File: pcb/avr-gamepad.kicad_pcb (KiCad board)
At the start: 2 copper layers, 53.2 x 53 mm, 36 parts, among them J1 Conn_01x08, J2 Conn_01x08, J3 Conn_01x05, P1 USB_C_Plug_USB2.0, SW1 RESET, SW10 Up, SW11 Down, SW12 Left, SW13 Select, SW14 HWB, SW2 R, SW3 X, SW4 A, SW5 B, SW6 Start, SW7 Y, SW8 Right, SW9 L, U1 ATmega32U4-AU, Y1 Crystal_GND24

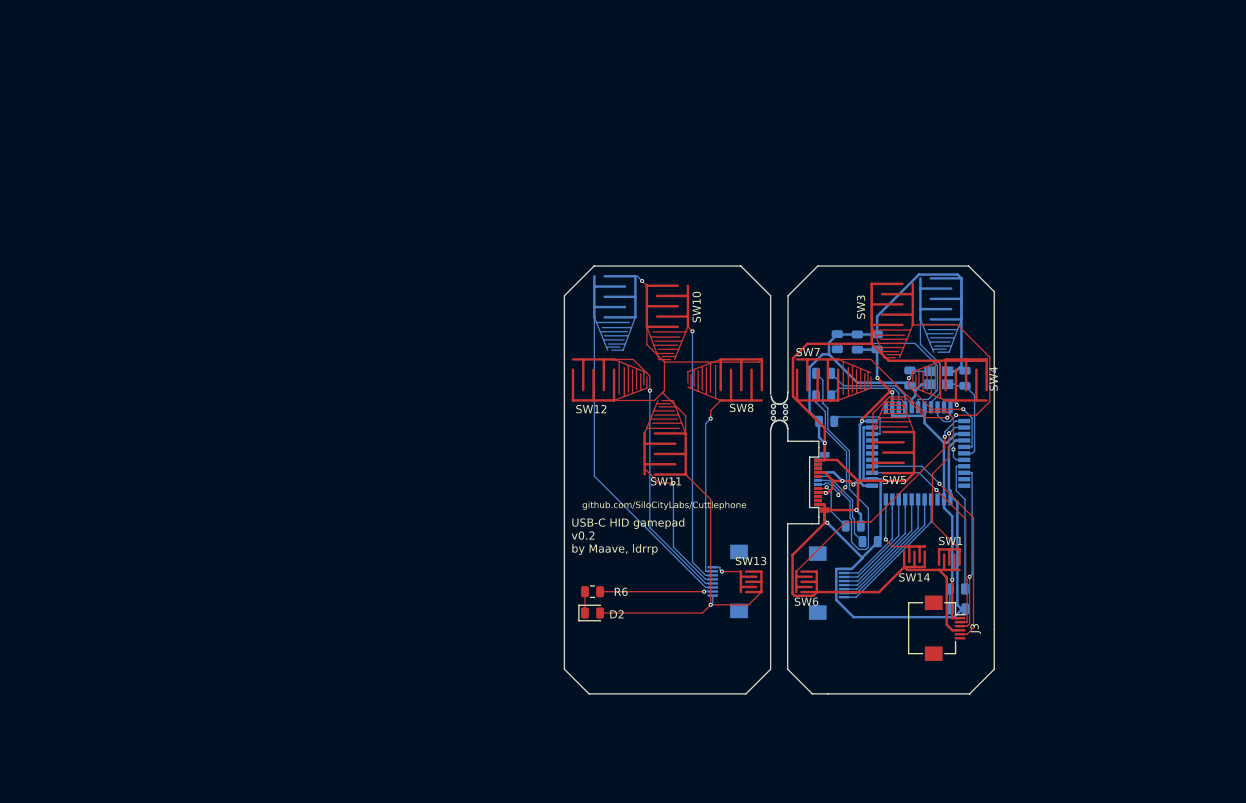
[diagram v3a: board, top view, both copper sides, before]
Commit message: change left/right on schematic, start arranging pcb, add pcf8574 footprint
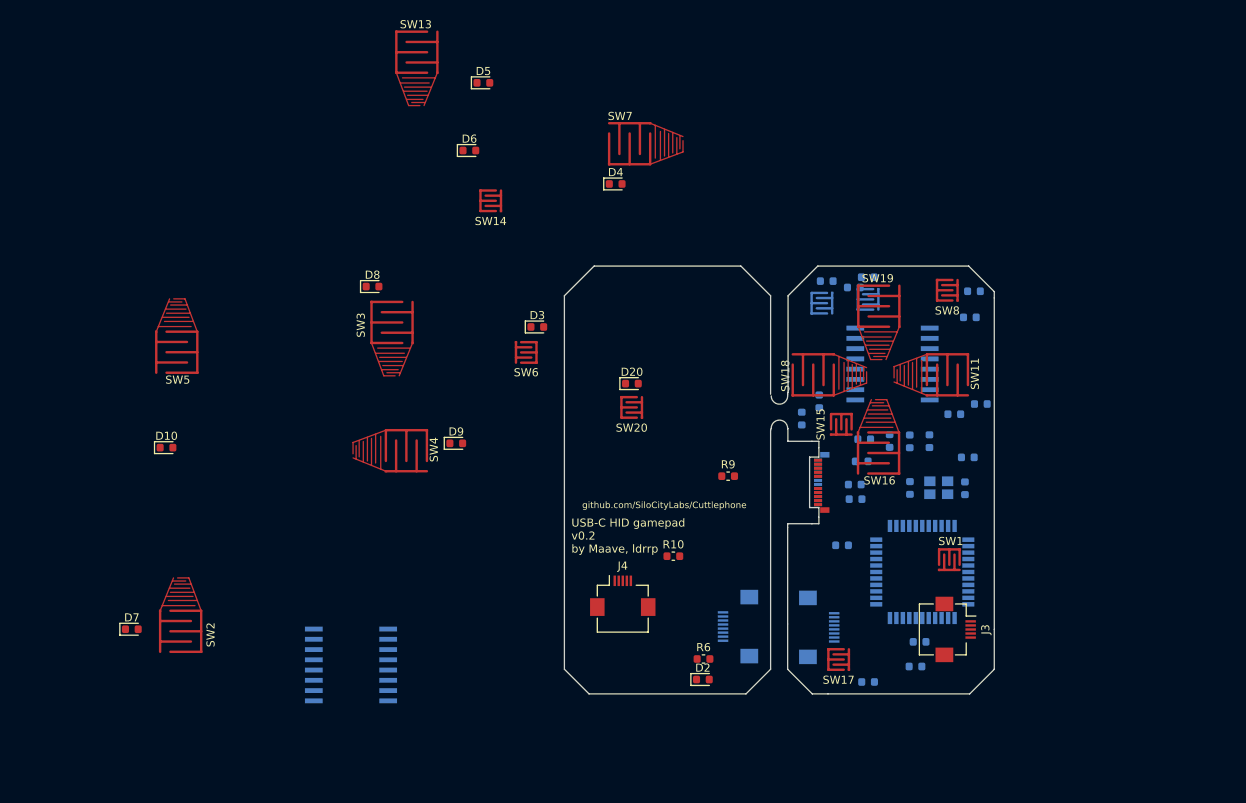
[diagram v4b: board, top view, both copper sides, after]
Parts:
- removed G***: LOGO, squidward:loser_silkscreen
- removed SW12: Left, button-contacts:Large_tapered
- removed mb-2mm-2: mb2, Panelization:mouse-bite-2mm-slot
- added D10: 1N4148, Diode_SMD:D_0603_1608Metric, F.Cu at (50.6, 102.9)
- added D11: 1N4148, Diode_SMD:D_0603_1608Metric, B.Cu at (137.4, 131.9)
- added D12: 1N4148, Diode_SMD:D_0603_1608Metric, B.Cu at (150.5, 83.5)
- added D13: 1N4148, Diode_SMD:D_0603_1608Metric, B.Cu at (132.3, 82.3)
- added D14: 1N4148, Diode_SMD:D_0603_1608Metric, B.Cu at (150.0, 86.7)
- added D15: 1N4148, Diode_SMD:D_0603_1608Metric, B.Cu at (148.1, 98.7)
- added D16: 1N4148, Diode_SMD:D_0603_1608Metric, B.Cu at (137.4, 81.8)
- added D17: 1N4148, Diode_SMD:D_0603_1608Metric, B.Cu at (135.6, 83.0)
- added D18: 1N4148, Diode_SMD:D_0603_1608Metric, B.Cu at (131.4, 97.1)
- added D19: 1N4148, Diode_SMD:D_0603_1608Metric, B.Cu at (129.2, 99.3)
- added D20: 1N4148, Diode_SMD:D_0603_1608Metric, F.Cu at (108.2, 94.9)
- added D3: 1N4148, Diode_SMD:D_0603_1608Metric, F.Cu at (96.5, 87.9)
- added D4: 1N4148, Diode_SMD:D_0603_1608Metric, F.Cu at (106.2, 70.2)
- added D5: 1N4148, Diode_SMD:D_0603_1608Metric, F.Cu at (89.8, 57.7)
- added D6: 1N4148, Diode_SMD:D_0603_1608Metric, F.Cu at (88.1, 66.1)
- added D7: 1N4148, Diode_SMD:D_0603_1608Metric, F.Cu at (46.3, 125.3)
- added D8: 1N4148, Diode_SMD:D_0603_1608Metric, F.Cu at (76.1, 82.9)
- added D9: 1N4148, Diode_SMD:D_0603_1608Metric, F.Cu at (86.4, 102.3)
- added J4: Conn_01x05, uxcell-ffc:uxcell_ffc_0.5pitch_1x05, F.Cu at (107.0, 121.2)
- added R10: 1K, Resistor_SMD:R_0603_1608Metric, F.Cu at (113.3, 116.3)
- added R7: 1K, Resistor_SMD:R_0603_1608Metric, B.Cu at (143.8, 126.9)
- added R8: 1K, Resistor_SMD:R_0603_1608Metric, B.Cu at (143.3, 130.0)
- added R9: 1K, Resistor_SMD:R_0603_1608Metric, F.Cu at (120.1, 106.4)
- added SW15: Custom4, button-contacts:Small, F.Cu at (134.1, 100.0)
- added SW16: B, button-contacts:Large_tapered, F.Cu at (138.7, 103.5)
- added SW17: Start, button-contacts:Small, F.Cu at (133.8, 129.1)
- added SW18: Y, button-contacts:Large_tapered, F.Cu at (130.6, 93.9)
- added SW19: X, button-contacts:Large_tapered, F.Cu at (138.7, 85.4)
- added SW20: Custom2, button-contacts:Small, F.Cu at (108.2, 97.9)
- added U2: PCF8574, pcf8574:SO16W, B.Cu at (73.4, 129.8)
- added U3: PCF8574, pcf8574:SO16W, B.Cu at (140.4, 92.5)
- C1, C2, C3, C4, C5, C6: footprint Capacitor_SMD:C_0805_2012Metric -> Capacitor_SMD:C_0603_1608Metric
- D1, D2: footprint LED_SMD:LED_0805_2012Metric -> LED_SMD:LED_0603_1608Metric
- J1, J2: value Conn_01x08 -> Conn_01x06
- J3: footprint Connector_FFC-FPC:Hirose_FH12-6S-0.5SH_1x06-1MP_P0.50mm_Horizontal -> uxcell-ffc:uxcell_ffc_0.5pitch_1x05
- R1, R2, R3, R4, R5, R6: footprint Resistor_SMD:R_0805_2012Metric -> Resistor_SMD:R_0603_1608Metric
- SW10: value Up -> R2; footprint button-contacts:Large_tapered -> button-contacts:Small; moved to B.Cu
- SW11: value Down -> A
- SW13: value Select -> Left; footprint button-contacts:Small -> button-contacts:Large_tapered
- SW14: value HWB -> L2
- SW2: value R -> Right; moved to F.Cu
- SW3: value X -> Up
- SW4: value A -> Down
- SW5: value B -> Custom1
- SW6: value Start -> Select
- SW7: value Y -> L1
- SW8: value Right -> R1; footprint button-contacts:Large_tapered -> button-contacts:Small
- SW9: value L -> Custom3; footprint button-contacts:Large_tapered -> button-contacts:Small
- moved SW2 102.7 mm to (52.3, 125.6)
- moved SW5 89.6 mm to (51.8, 91.1)
- moved SW13 77.5 mm to (81.6, 53.9), turned to 0 degrees
- moved SW4 69.8 mm to (80.3, 103.3)
- moved SW14 68.5 mm to (90.7, 72.3), turned to 0 degrees
- moved SW3 62.0 mm to (78.5, 87.4)
- moved SW6 44.8 mm to (95.1, 91.1)
- moved SW7 37.4 mm to (107.9, 65.3)
- moved SW11 36.3 mm to (147.2, 93.9), turned to 270 degrees
- moved SW9 31.3 mm to (137.4, 84.5), turned to 0 degrees
- moved SW8 27.8 mm to (147.2, 83.4), turned to 0 degrees
- moved R5 23.1 mm to (151.4, 97.5)
- moved SW10 19.1 mm to (131.7, 85.0)
- moved D1 18.8 mm to (149.8, 104.1)
- moved R6 16.1 mm to (117.0, 129.0)
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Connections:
- net /pd3-21 renamed Net-(U1-Pad21)
- net /pd4-25 renamed Net-(U1-Pad25)
- net /pd5-22 renamed Net-(U1-Pad22)
- net /pe6-1 renamed Net-(U1-Pad1)
- net /pf0-41 renamed Net-(U1-Pad41)
- net /pf1-40 renamed Net-(U1-Pad40)
- net /pf6-37 renamed /JoyRightX
- net /pf7-36 renamed /JoyRightY
- net Net-(R1-Pad1) renamed /D+
- net Net-(R2-Pad1) renamed /D-
- D2 pad 2: Net-(D2-Pad2) -> /GND_L
- J1 pad 1: Net-(J1-Pad1) -> /SDA_L
- J1 pad 2: Net-(J1-Pad2) -> /SCL_L
- J1 pad 3: Net-(J1-Pad3) -> /JoyLeftX_L
- J1 pad 4: Net-(J1-Pad4) -> /JoyLeftY_L
- J1 pad 5: Net-(J1-Pad5) -> /VCC_L
- J1 pad 6: Net-(J1-Pad6) -> /GND_L
- J1 pad 7: Net-(J1-Pad7) -> (no net)
- J1 pad 8: Net-(D2-Pad2) -> (no net)
- J2 pad 1: /pd6-26 -> /SDA
- J2 pad 2: /pd7-27 -> /SCL
- J2 pad 3: /pb4-28 -> /JoyLeftX
- J2 pad 4: /pb5-29 -> /JoyLeftY
- J2 pad 5: /pb6-30 -> +5V
- J2 pad 6: /pc6-31 -> GND
- J2 pad 7: /pc7-32 -> (no net)
- J2 pad 8: GND -> (no net)
- J3 pad 3: /pd2-20 -> /R3
- P1 pad A6: Net-(P1-PadA6) -> Net-(P1-PadA5)
- R1 pad 2: Net-(P1-PadA6) -> Net-(P1-PadA5)
- R5 pad 2: /pd1-19 -> Net-(R5-Pad2)
- R6 pad 2: Net-(J1-Pad7) -> Net-(R6-Pad2)
- SW10 pad 1: Net-(J1-Pad3) -> /Col1
- SW10 pad 2: Net-(D2-Pad2) -> Net-(D13-Pad2)
- SW11 pad 1: Net-(J1-Pad4) -> /Col2
- SW11 pad 2: Net-(D2-Pad2) -> Net-(D14-Pad2)
- SW13 pad 1: Net-(J1-Pad1) -> /ColL1
- SW13 pad 2: Net-(D2-Pad2) -> Net-(D5-Pad2)
- SW14 pad 1: Net-(SW14-Pad1) -> /ColL1
- SW14 pad 2: GND -> Net-(D6-Pad2)
- SW2 pad 1: /pb0-8 -> /ColL3
- SW2 pad 2: GND -> Net-(D7-Pad2)
- SW3 pad 1: /pb1-9 -> /ColL2
- SW3 pad 2: GND -> Net-(D8-Pad2)
- SW4 pad 1: /pb2-10 -> /ColL2
- SW4 pad 2: GND -> Net-(D9-Pad2)
- SW5 pad 1: /pb3-11 -> /ColL2
- SW5 pad 2: GND -> Net-(D10-Pad2)
- SW6 pad 1: /pb7-12 -> /ColL3
- SW6 pad 2: GND -> Net-(D3-Pad2)
- SW7 pad 1: /pd0-18 -> /ColL1
- SW7 pad 2: GND -> Net-(D4-Pad2)
- SW8 pad 1: Net-(J1-Pad2) -> /Col1
- SW8 pad 2: Net-(D2-Pad2) -> Net-(D12-Pad2)
- SW9 pad 1: Net-(J1-Pad6) -> /Col2
- SW9 pad 2: Net-(D2-Pad2) -> Net-(D16-Pad2)
- U1 pad 10: /pb2-10 -> Net-(U1-Pad10)
- U1 pad 11: /pb3-11 -> Net-(U1-Pad11)
- U1 pad 12: /pb7-12 -> Net-(U1-Pad12)
- U1 pad 18: /pd0-18 -> /SCL
- U1 pad 19: /pd1-19 -> /SDA
- U1 pad 20: /pd2-20 -> Net-(U1-Pad20)
- U1 pad 26: /pd6-26 -> Net-(U1-Pad26)
- U1 pad 27: /pd7-27 -> Net-(U1-Pad27)
- U1 pad 28: /pb4-28 -> Net-(U1-Pad28)
- U1 pad 29: /pb5-29 -> Net-(U1-Pad29)
- U1 pad 30: /pb6-30 -> Net-(U1-Pad30)
- U1 pad 31: /pc6-31 -> Net-(U1-Pad31)
- U1 pad 32: /pc7-32 -> Net-(U1-Pad32)
- U1 pad 33: Net-(SW14-Pad1) -> Net-(U1-Pad33)
- U1 pad 38: /pf5-38 -> /JoyLeftY
- U1 pad 39: /pf4-39 -> /JoyLeftX
- U1 pad 8: /pb0-8 -> Net-(U1-Pad8)
- U1 pad 9: /pb1-9 -> Net-(U1-Pad9)
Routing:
- net GND: track 260.7 -> 0.00 mm, vias 3 -> 0
- net Net-(D2-Pad2): track 90.8 -> 0.00 mm, vias 2 -> 0
- net +5V: track 76.1 -> 0.00 mm, vias 7 -> 0
- net Net-(J1-Pad6): track 40.0 -> 0.00 mm
- net Net-(P1-PadA6): track 36.9 -> 0.00 mm
- net Net-(J1-Pad5): track 34.7 -> 0.00 mm, vias 1 -> 0
- net Net-(J1-Pad3): track 32.6 -> 0.00 mm, vias 1 -> 0
- net /JoyRightX: track 30.8 -> 0.00 mm, vias 1 -> 0
- net /pb7-12: track 29.7 -> 0.00 mm, vias 1 -> 0
- net /JoyRightY: track 27.7 -> 0.00 mm, vias 1 -> 0
- net /pb1-9: track 25.5 -> 0.00 mm, vias 1 -> 0
- net /pd0-18: track 23.6 -> 0.00 mm, vias 1 -> 0
- net Net-(J1-Pad4): track 23.1 -> 0.00 mm, vias 1 -> 0
- net Net-(J1-Pad2): track 22.8 -> 0.00 mm, vias 1 -> 0
- net /pd2-20: track 21.1 -> 0.00 mm, vias 1 -> 0
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
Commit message: disabled extra buttons, fixed R-L conversion
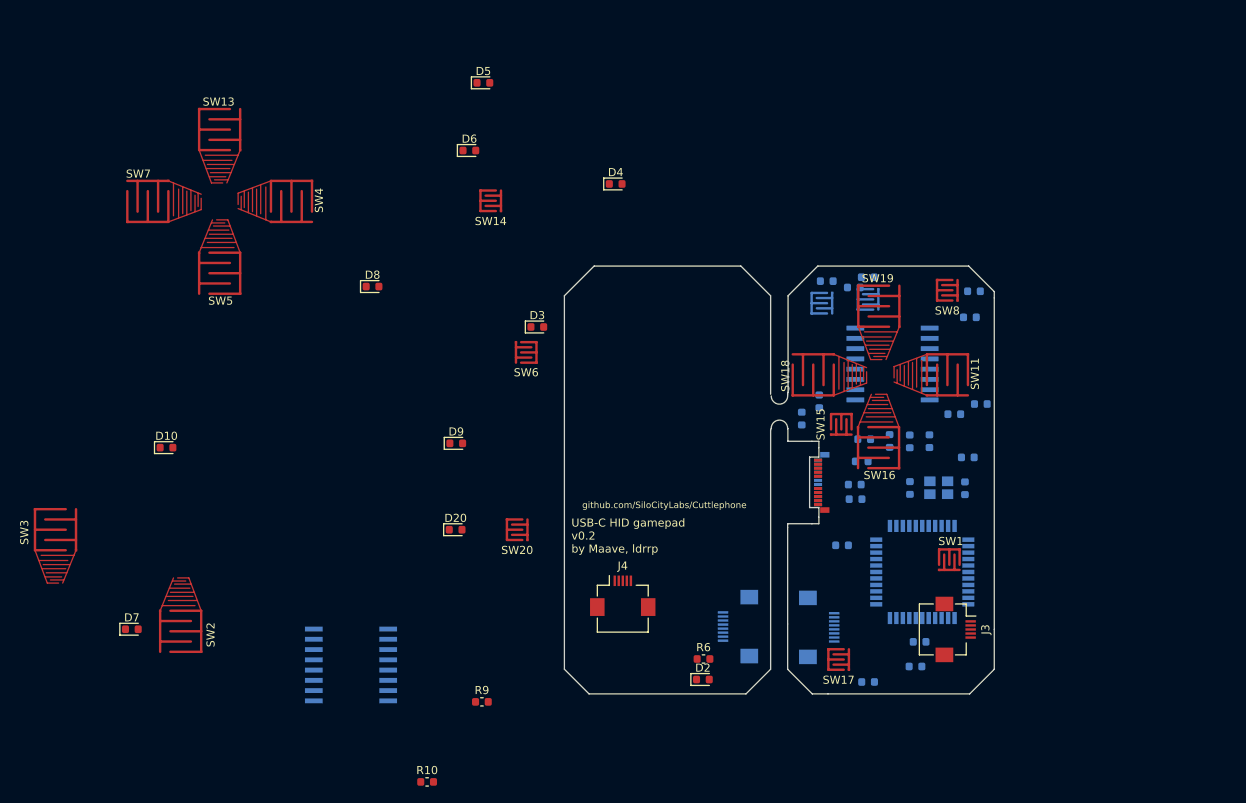
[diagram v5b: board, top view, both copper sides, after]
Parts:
- moved SW7 60.1 mm to (48.3, 72.4)
- moved SW3 48.9 mm to (36.8, 113.0)
- moved R10 41.3 mm to (82.8, 144.2)
- moved R9 41.3 mm to (89.6, 134.3)
- moved SW4 34.0 mm to (66.0, 72.4)
- moved D20 28.3 mm to (86.4, 113.0)
- moved SW13 26.2 mm to (57.1, 63.5)
- moved SW20 20.7 mm to (94.0, 113.0)
- moved SW5 11.1 mm to (57.1, 81.3)
- moved SW16 0.67 mm to (138.7, 102.9)
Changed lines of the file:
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@@
-(kicad_pcb (version 20171130) (host pcbnew "(5.1.2)-1")
+(kicad_pcb (version 20171130) (host pcbnew 5.1.5-52549c5~86~ubuntu18.04.1)
   (general
     (thickness 0.1016)
@@
   )
   (module button-contacts:Large_tapered (layer F.Cu)
-    (at 78.486 87.376)
+    (at 36.83 113.03)
     (attr smd)
     (fp_text reference SW3 (at -3.8352 0.3304 90) (layer F.SilkS)
@@
   )
   (module button-contacts:Large_tapered (layer F.Cu)
-    (at 80.264 103.251 270)
+    (at 66.04 72.39 270)
     (attr smd)
     (fp_text reference SW4 (at -0.127 -3.429 90) (layer F.SilkS)
@@
   )
   (module button-contacts:Large_tapered (layer F.Cu)
-    (at 107.8992 65.2526 90)
+    (at 48.26 72.39 90)
     (attr smd)
     (fp_text reference SW7 (at 3.4036 -1.1688 180) (layer F.SilkS)
@@
   )
   (module Diode_SMD:D_0603_1608Metric (layer F.Cu)
-    (at 108.1785 94.9452)
+    (at 86.36 113.03)
     (descr "Diode SMD 0603 (1608 Metric), square (rectangular) end terminal, IPC_7351 nominal, (Body size source: http://www.tortai-tech.com/upload/download/2011102023233369053.pdf), generated with kicad-footprint-generator")
     (tags diode)
@@
   )
   (module button-contacts:Large_tapered (layer F.Cu)
-    (at 138.7094 103.53548 180)
+    (at 138.7094 102.87 180)
     (attr smd)
     (fp_text reference SW16 (at -0.127 -3.429) (layer F.SilkS)
@@
   )
   (module button-contacts:Small (layer F.Cu)
-    (at 108.1532 97.8916)
+    (at 93.98 113.03)
     (attr smd)
     (fp_text reference SW20 (at 0 2.54) (layer F.SilkS)
@@
   )
   (module button-contacts:Large_tapered (layer F.Cu)
-    (at 51.8414 91.059 180)
+    (at 57.15 81.28 180)
     (attr smd)
     (fp_text reference SW5 (at -0.127 -3.429) (layer F.SilkS)
@@
   )
   (module Resistor_SMD:R_0603_1608Metric (layer F.Cu)
-    (at 120.0913 106.4006)
+    (at 89.6113 134.3406)
     (descr "Resistor SMD 0603 (1608 Metric), square (rectangular) end terminal, IPC_7351 nominal, (Body size source: http://www.tortai-tech.com/upload/download/2011102023233369053.pdf), generated with kicad-footprint-generator")
     (tags resistor)
@@
   )
   (module Resistor_SMD:R_0603_1608Metric (layer F.Cu)
-    (at 113.3095 116.3066)
+    (at 82.8295 144.2466)
     (descr "Resistor SMD 0603 (1608 Metric), square (rectangular) end terminal, IPC_7351 nominal, (Body size source: http://www.tortai-tech.com/upload/download/2011102023233369053.pdf), generated with kicad-footprint-generator")
     (tags resistor)
@@
   )
   (module button-contacts:Large_tapered (layer F.Cu)
-    (at 81.5594 53.9242)
+    (at 57.15 63.5)
     (attr smd)
     (fp_text reference SW13 (at -0.127 -3.429) (layer F.SilkS)

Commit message: swap left/right board sides for fab assembly
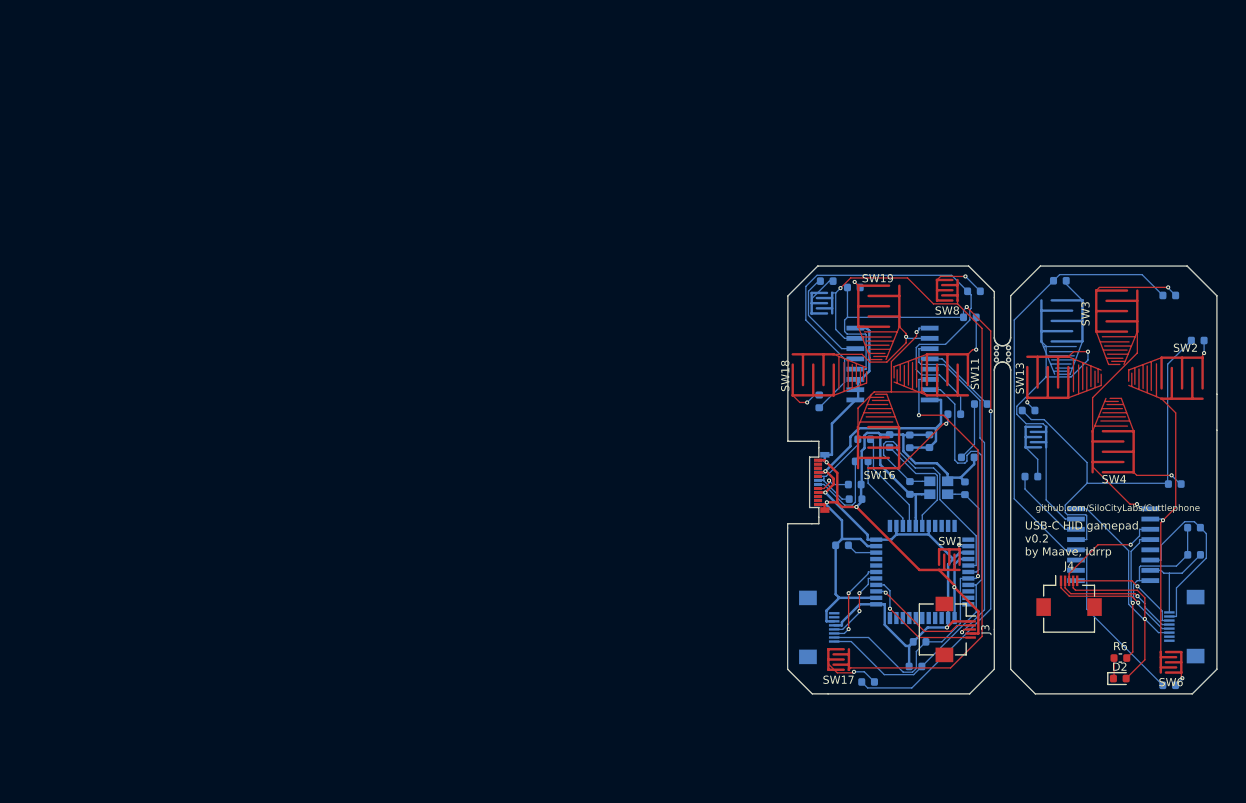
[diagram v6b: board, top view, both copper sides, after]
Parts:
- removed D10, D16, D19, D20: 1N4148, Diode_SMD:D_0603_1608Metric
- removed SW15: Custom4, button-contacts:Small
- removed SW20: Custom2, button-contacts:Small
- removed SW5: Custom1, button-contacts:Large_tapered
- removed SW9: Custom3, button-contacts:Small
- added mouse-bite-2mm-slot: VAL**, Panelization:mouse-bite-2mm-slot, F.Cu at (154.1, 91.3)
- D3, D4, D5, D6, D7, D8, D9, R10, R9, SW14, SW7: moved to B.Cu
- moved D7 136.7 mm to (178.2, 89.6)
- moved SW3 134.1 mm to (168.2, 86.0)
- moved SW2 127.9 mm to (176.3, 94.3), turned to 270 degrees
- moved SW7 114.1 mm to (161.4, 87.2), turned to 180 degrees
- moved SW13 107.0 mm to (159.7, 94.2), turned to 90 degrees
- moved SW4 106.3 mm to (167.7, 103.4), turned to 180 degrees
- moved R10 100.0 mm to (177.8, 112.8)
- moved D8 98.6 mm to (174.7, 84.0)
- moved U2 95.5 mm to (167.7, 114.9)
- moved R9 90.0 mm to (177.8, 116.1)
- moved D3 89.9 mm to (174.7, 132.3)
- moved D9 89.1 mm to (175.4, 107.4)
- moved SW6 88.6 mm to (174.9, 129.4)
- moved D6 80.4 mm to (157.6, 106.5)
- moved D5 78.7 mm to (157.3, 98.3)
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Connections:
- J4 pad 4: /GND_R -> /GND_L
- R10 pad 1: /VCC_R -> /VCC_L
- R9 pad 1: /VCC_R -> /VCC_L
- U2 pad 16: /VCC_R -> /VCC_L
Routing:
- net GND: track 0.00 -> 144.5 mm, vias 0 -> 4
- net +5V: track 0.00 -> 93.1 mm, vias 0 -> 3
- net /Row1: track 0.00 -> 88.8 mm, vias 0 -> 2
- net /Col1: track 0.00 -> 86.1 mm, vias 0 -> 1
- net /RowL1: track 0.00 -> 76.2 mm
- net /Row2: track 0.00 -> 64.7 mm
- net /SCL: track 0.00 -> 59.5 mm, vias 0 -> 2
- net /SDA: track 0.00 -> 58.6 mm
- net /RowL2: track 0.00 -> 54.1 mm
- net /R3: track 0.00 -> 43.9 mm, vias 0 -> 1
- net /GND_L: track 0.00 -> 43.0 mm, vias 0 -> 1
- net /ColL1: track 0.00 -> 38.5 mm, vias 0 -> 1
- net /ColL3: track 0.00 -> 34.5 mm, vias 0 -> 1
- net /VCC_L: track 0.00 -> 32.9 mm, vias 0 -> 1
- net Net-(C4-Pad1): track 0.00 -> 31.7 mm
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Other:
- board size 53.2 x 53 mm -> 53.1 x 53 mm

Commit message: board edge cuts for joystick
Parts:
- J3, J4: moved to B.Cu
- moved J4 23.4 mm to (175.9, 102.2), turned to 180 degrees
- moved J3 23.0 mm to (148.2, 102.4), turned to 180 degrees
- moved D9 12.6 mm to (162.8, 107.9)
- moved D1 9.60 mm to (150.3, 113.7), turned to 180 degrees
- moved D15 7.64 mm to (140.6, 100.1)
- moved C6 6.17 mm to (138.8, 108.1)
- moved R7 4.74 mm to (145.8, 131.2)
- moved C2 4.23 mm to (142.5, 105.5)
- moved C1 3.81 mm to (140.8, 105.5)
- moved U2 3.77 mm to (164.0, 115.1)
- moved C3 3.61 mm to (147.7, 111.1)
- moved C4 3.61 mm to (140.9, 111.1)
- moved Y1 3.61 mm to (144.5, 111.0)
- moved C5 3.56 mm to (134.6, 118.5)
- moved U1 3.41 mm to (144.6, 121.6)
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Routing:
- net /SDA_L: track 12.2 -> 42.7 mm
- net /R3: track 43.9 -> 17.2 mm, vias 1 -> 0
- net /GND_L: track 43.0 -> 64.1 mm
- net /JoyRightX: track 15.7 -> 36.4 mm, vias 1 -> 2
- net /SCL_L: track 23.3 -> 42.4 mm
- net /Row1: track 88.8 -> 69.9 mm
- net Net-(D1-Pad1): track 7.27 -> 25.2 mm, vias 0 -> 2
- net /JoyLeftX_L: track 14.1 -> 31.0 mm, vias 1 -> 2
- net /VCC_L: track 32.9 -> 49.8 mm, vias 1 -> 0
- net /JoyRightY: track 14.0 -> 30.0 mm, vias 1 -> 2
- net /JoyLeftY_L: track 15.9 -> 29.5 mm, vias 1 -> 2
- net /RowL2: track 54.1 -> 65.6 mm
- net Net-(C4-Pad1): track 31.7 -> 22.1 mm
- net /ColL1: track 38.5 -> 29.1 mm
- net /SCL: track 59.5 -> 67.1 mm, vias 2 -> 0
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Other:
- outline, holes or cut-outs redrawn
